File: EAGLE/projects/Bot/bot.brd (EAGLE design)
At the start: 122 x 94.9 mm, 19 parts, among them IC1 7805T, U3 ARDUINO_SHIELDLABEL

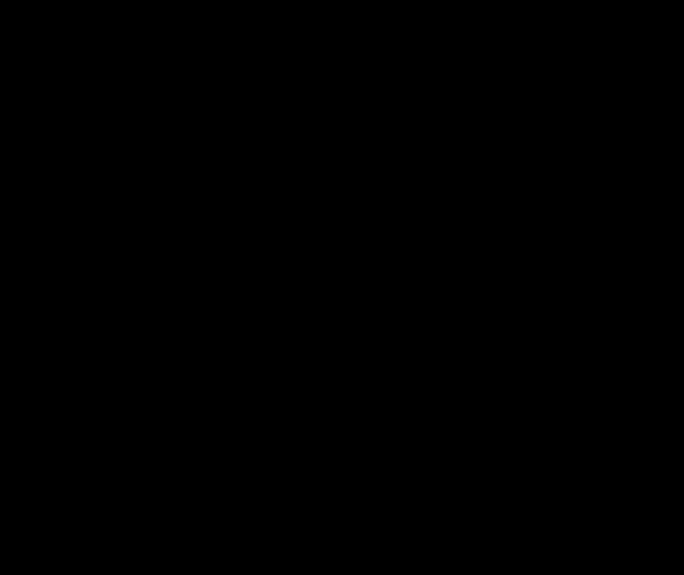
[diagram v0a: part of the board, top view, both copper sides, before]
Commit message: add blinker LED
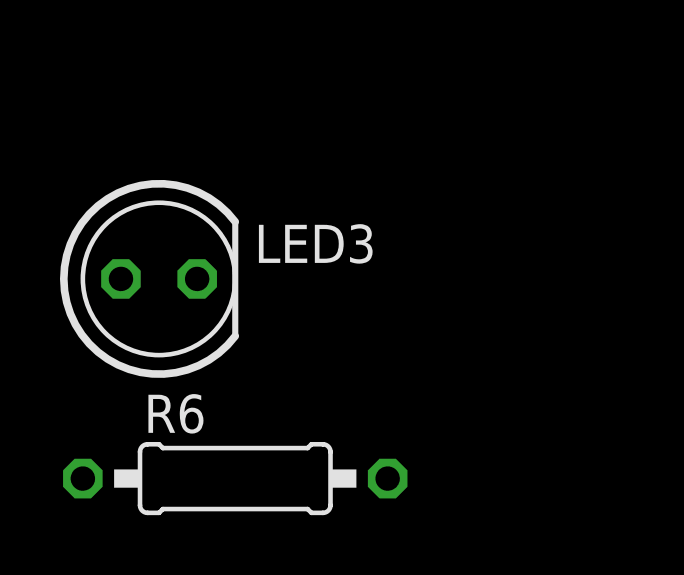
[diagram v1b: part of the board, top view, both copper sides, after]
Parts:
- added LED3: (no value), led:LED5MM
- added R6: 100, resistor:0207/10
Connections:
- new net N$4: LED3.A, PI.22
- new net N$6: LED3.K, R6.2
- net 0: now also R6.1
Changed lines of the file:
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@@
 <attribute name="VALUE" x="30.5562" y="21.1836" size="1.778" layer="27" ratio="10" rot="R180"/>
+</element>
+<element name="LED3" library="led" library_urn="urn:adsk.eagle:library:259" package="LED5MM" package3d_urn="urn:adsk.eagle:package:15799/2" value="" x="0.7112" y="-10.3124" smashed="yes">
+<attribute name="NAME" x="3.8862" y="-9.779" size="1.27" layer="25" ratio="10"/>
+<attribute name="POPULARITY" value="93" x="0.7112" y="-10.3124" size="1.778" layer="27" display="off"/>
+<attribute name="VALUE" x="3.9116" y="-12.1158" size="1.27" layer="27" ratio="10"/>
+</element>
+<element name="R6" library="resistor" library_urn="urn:adsk.eagle:library:348" package="0207/10" package3d_urn="urn:adsk.eagle:package:25939/1" value="100" x="3.2512" y="-16.9672" smashed="yes">
+<attribute name="NAME" x="0.2032" y="-15.4432" size="1.27" layer="25" ratio="10"/>
+<attribute name="VALUE" x="0.9906" y="-17.6022" size="1.27" layer="27" ratio="10"/>
 </element>
 </elements>
@@
 <wire x1="102.235" y1="25.4" x2="110.49" y2="25.4" width="0.3048" layer="16"/>
 <wire x1="26.035" y1="10.795" x2="25.5016" y2="11.0744" width="0.3048" layer="16"/>
+<contactref element="R6" pad="1"/>
+<wire x1="-1.8288" y1="-16.9672" x2="25.5016" y2="11.0744" width="0" layer="19" extent="1-1"/>
 </signal>
 <signal name="L_FWD">
@@
 </polygon>
 </signal>
+<signal name="N$4">
+<contactref element="PI" pad="22"/>
+<contactref element="LED3" pad="A"/>
+<wire x1="-0.5588" y1="-10.3124" x2="53.2366" y2="63.4118" width="0" layer="19" extent="1-1"/>
+</signal>
+<signal name="N$6">
+<contactref element="LED3" pad="K"/>
+<contactref element="R6" pad="2"/>
+<wire x1="8.3312" y1="-16.9672" x2="1.9812" y2="-10.3124" width="0" layer="19" extent="1-1"/>
+</signal>
 </signals>

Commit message: git
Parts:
- added S1: (no value), switch1:MS243
- moved R6 117.9 mm to (112.0, 28.5), turned to 90 degrees
- moved LED3 74.8 mm to (62.2, 32.2)
- moved JP7 4.80 mm to (107.5, 85.5)
- moved KK1 3.03 mm to (28.4, 14.4)
- moved IC1 3.03 mm to (28.4, 22.0)
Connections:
- new net N$3: JP2.1, S1.1
- net 0: now also S1.2; no longer JP2.1
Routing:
- net N$3: track 0.00 -> 77.8 mm
- net PI_5V: track 263.3 -> 317.0 mm
- net N$6: track 0.00 -> 52.3 mm, vias 0 -> 2
- net PI_3V3: track 79.8 -> 120.1 mm
- net N$4: track 0.00 -> 34.5 mm, vias 0 -> 2
- net 0: track 501.5 -> 477.6 mm
- net PWR+: track 241.3 -> 233.2 mm
- net L_SPD: track 53.2 -> 49.2 mm
- net R_SPD: track 93.6 -> 91.6 mm
- added copper zone on layer 16, net 0
- removed copper zone on layer 16, net N$3
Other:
- board size 122 x 94.9 mm -> 122.5 x 95 mm

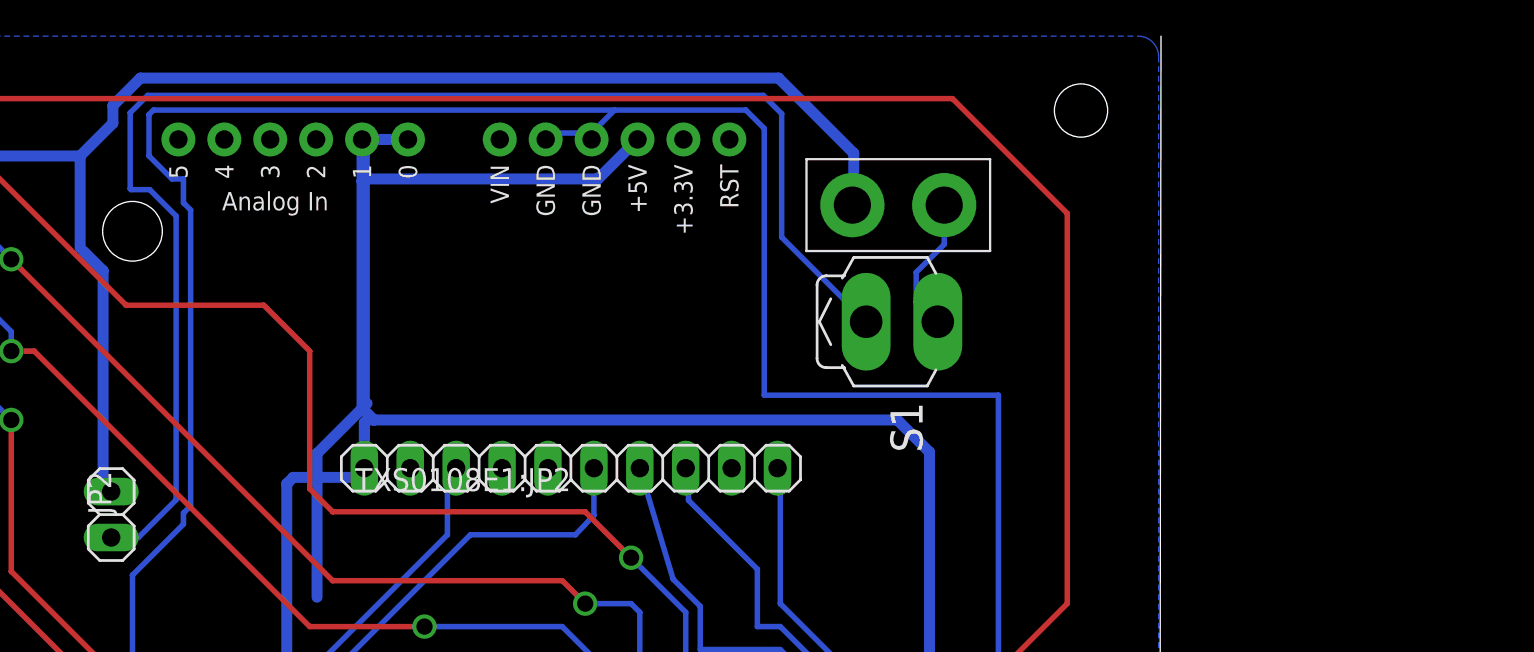
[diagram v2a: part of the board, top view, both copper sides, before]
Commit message: fixed switch position
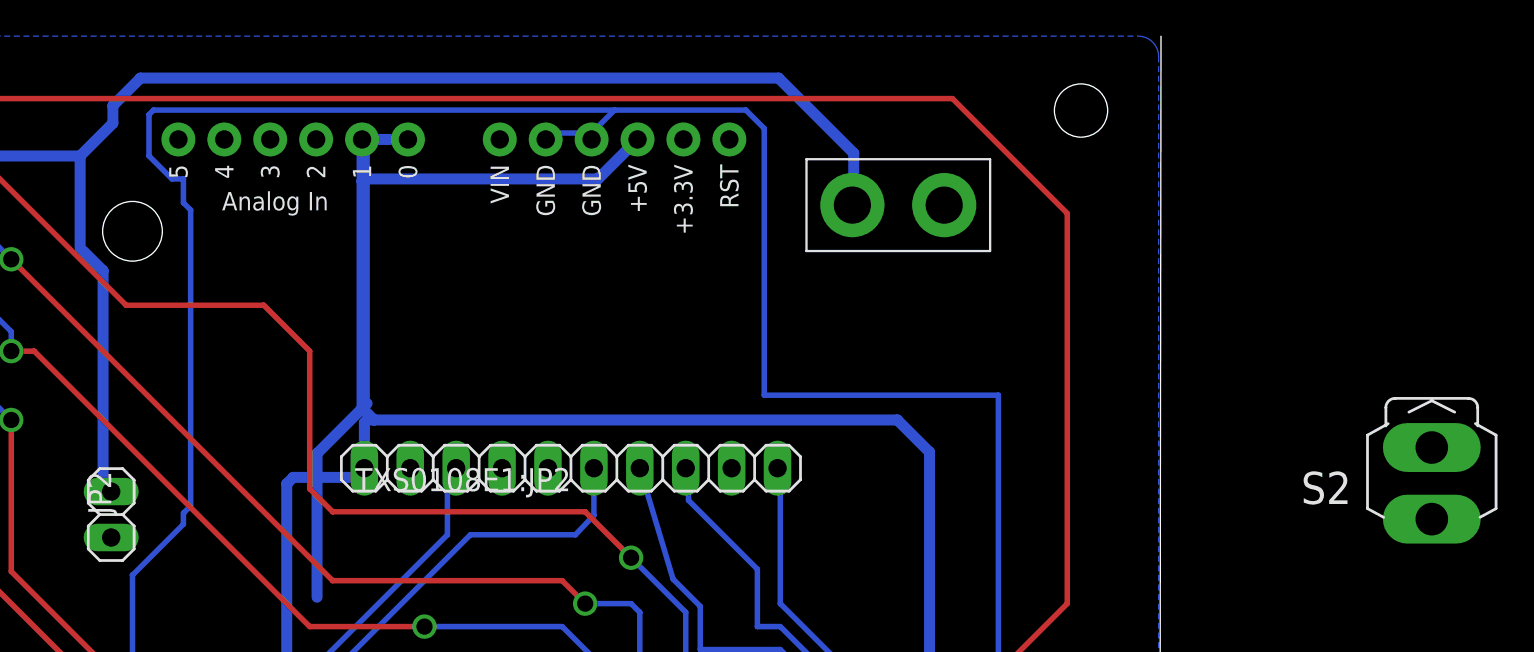
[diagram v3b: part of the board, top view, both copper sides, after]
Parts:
- removed S1: (no value), switch1:MS243
- added S2: (no value), switch1:MS243
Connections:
- removed net N$3: JP2.1, S1.1
- new net N$7: JP7.2, S2.1
- net 0: now also JP2.1, S2.2; no longer JP7.2, S1.2
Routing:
- net N$3: track 77.8 -> 0.00 mm
- net 0: track 477.6 -> 470.0 mm
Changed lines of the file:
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@@
 <attribute name="VALUE" x="112.6236" y="26.2128" size="1.27" layer="27" ratio="10" rot="R90"/>
 </element>
-<element name="S1" library="switch1" package="MS243" package3d_urn="urn:adsk.eagle:package:27683/1" value="" x="108.331" y="79.0956" smashed="yes" rot="R270">
-<attribute name="NAME" x="107.061" y="74.6506" size="1.778" layer="25" ratio="10" rot="R270"/>
-<attribute name="POPULARITY" value="3" x="108.331" y="79.0956" size="1.778" layer="27" rot="R270" display="off"/>
-<attribute name="VALUE" x="104.521" y="74.6506" size="1.778" layer="27" ratio="10" rot="R270"/>
+<element name="S2" library="switch1" package="MS243" package3d_urn="urn:adsk.eagle:package:27683/1" value="" x="137.0076" y="69.5198" smashed="yes" rot="R180">
+<attribute name="NAME" x="132.5626" y="70.7898" size="1.778" layer="25" ratio="10" rot="R180"/>
+<attribute name="POPULARITY" value="3" x="137.0076" y="69.5198" size="1.778" layer="27" rot="R180" display="off"/>
+<attribute name="VALUE" x="132.5626" y="73.3298" size="1.778" layer="27" ratio="10" rot="R180"/>
 </element>
 </elements>
@@
 <contactref element="U$2" pad="4"/>
 <contactref element="R5" pad="1"/>
-<contactref element="JP7" pad="2"/>
 <contactref element="U3" pad="GND@2"/>
 <contactref element="U3" pad="GND@1"/>
@@
 <wire x1="65.1256" y1="65.0748" x2="65.1256" y2="54.9656" width="0.3048" layer="16"/>
 <wire x1="53.34" y1="43.18" x2="65.1256" y2="54.9656" width="0.3048" layer="16"/>
-<contactref element="S1" pad="2"/>
-<wire x1="108.4834" y1="81.825725" x2="108.4834" y2="80.175475" width="0.3048" layer="16"/>
-<wire x1="108.4834" y1="80.175475" x2="108.572675" y2="80.0862" width="0.3048" layer="16"/>
-<wire x1="110.0328" y1="85.5472" x2="110.0328" y2="83.375125" width="0.3048" layer="16"/>
-<wire x1="110.0328" y1="83.375125" x2="108.4834" y2="81.825725" width="0.3048" layer="16"/>
-<wire x1="108.572675" y1="80.0862" x2="108.6866" y2="80.0862" width="0.3048" layer="16"/>
-<wire x1="108.6866" y1="80.0862" x2="109.6772" y2="79.0956" width="0.3048" layer="16"/>
 <wire x1="67.945" y1="67.8942" x2="65.1256" y2="65.0748" width="0.3048" layer="16"/>
 <wire x1="66.2891625" y1="90.805" x2="91.7956" y2="90.805" width="0.3048" layer="16"/>
@@
 <wire x1="90.5256" y1="89.1794" x2="90.5256" y2="89.535" width="0.3048" layer="16"/>
 <wire x1="90.5256" y1="89.535" x2="91.7956" y2="90.805" width="0.3048" layer="16"/>
-<wire x1="100.8126" y1="70.993" x2="109.6772" y2="79.0956" width="0" layer="19" extent="1-1"/>
+<contactref element="S2" pad="2"/>
+<contactref element="JP2" pad="1"/>
+<wire x1="100.8126" y1="70.993" x2="137.0076" y2="68.1736" width="0" layer="19" extent="1-1"/>
 <wire x1="111.9886" y1="23.3934" x2="96.1898" y2="23.3172" width="0" layer="19" extent="1-1"/>
+<wire x1="63.948453125" y1="67.1576" x2="65.1256" y2="65.1002" width="0" layer="19" extent="16-16"/>
 </signal>
 <signal name="L_FWD">
@@
 <wire x1="66.3956" y1="35.052" x2="63.5" y2="32.1564" width="0.3048" layer="16"/>
 </signal>
-<signal name="N$3">
-<contactref element="S1" pad="1"/>
-<contactref element="JP2" pad="1"/>
-<wire x1="105.7148" y1="79.0956" x2="101.0412" y2="83.7692" width="0.3048" layer="16"/>
-<wire x1="101.0412" y1="83.7692" x2="101.0412" y2="90.6018" width="0.3048" layer="16"/>
-<wire x1="101.0412" y1="90.6018" x2="100.0252" y2="91.6178" width="0.3048" layer="16"/>
-<wire x1="65.9638" y1="91.6178" x2="64.9986" y2="90.6526" width="0.3048" layer="16"/>
-<wire x1="64.9986" y1="90.6526" x2="64.9986" y2="86.4536" width="0.3048" layer="16"/>
-<wire x1="64.9986" y1="86.4536" x2="65.0494" y2="86.4028" width="0.3048" layer="16"/>
-<wire x1="65.0494" y1="86.4028" x2="66.0797" y2="86.4028" width="0.3048" layer="16"/>
-<wire x1="65.4558" y1="67.1576" x2="63.948453125" y2="67.1576" width="0.3048" layer="16"/>
-<wire x1="100.0252" y1="91.6178" x2="65.9638" y2="91.6178" width="0.3048" layer="16"/>
-<wire x1="66.0797" y1="86.4028" x2="67.5386" y2="84.9439" width="0.3048" layer="16"/>
-<wire x1="67.5386" y1="84.9439" x2="67.5386" y2="69.2404" width="0.3048" layer="16"/>
-<wire x1="67.5386" y1="69.2404" x2="65.4558" y2="67.1576" width="0.3048" layer="16"/>
+<signal name="N$7">
+<contactref element="JP7" pad="2"/>
+<contactref element="S2" pad="1"/>
+<wire x1="110.0328" y1="85.5472" x2="137.0076" y2="72.136" width="0" layer="19" extent="1-1"/>
 </signal>
 </signals>

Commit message: Shoot me!
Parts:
- S2: device switch1:MS243 -> switch2:MS243
- moved S2 32.2 mm to (106.2, 78.9), turned to 90 degrees
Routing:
- net PI_5V: track 317.0 -> 305.1 mm
- net N$7: track 0.00 -> 11.1 mm
- net 0: track 470.0 -> 473.7 mm
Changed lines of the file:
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@@
 <setting verticaltext="up"/>
 </settings>
-<grid distance="1" unitdist="mil" unit="mil" style="lines" multiple="1" display="no" altdistance="5" altunitdist="mil" altunit="mil"/>
+<grid distance="20" unitdist="mil" unit="mil" style="lines" multiple="1" display="no" altdistance="5" altunitdist="mil" altunit="mil"/>
 <layers>
 <layer number="1" name="Top" color="4" fill="1" visible="yes" active="yes"/>
@@
 <attribute name="VALUE" x="112.6236" y="26.2128" size="1.27" layer="27" ratio="10" rot="R90"/>
 </element>
-<element name="S2" library="switch1" package="MS243" package3d_urn="urn:adsk.eagle:package:27683/1" value="" x="137.0076" y="69.5198" smashed="yes" rot="R180">
-<attribute name="NAME" x="132.5626" y="70.7898" size="1.778" layer="25" ratio="10" rot="R180"/>
-<attribute name="POPULARITY" value="3" x="137.0076" y="69.5198" size="1.778" layer="27" rot="R180" display="off"/>
-<attribute name="VALUE" x="132.5626" y="73.3298" size="1.778" layer="27" ratio="10" rot="R180"/>
+<element name="S2" library="switch2" package="MS243" package3d_urn="urn:adsk.eagle:package:27683/1" value="" x="106.2228" y="78.9432" smashed="yes" rot="R90">
+<attribute name="NAME" x="107.4928" y="83.3882" size="1.778" layer="25" ratio="10" rot="R90"/>
+<attribute name="POPULARITY" value="3" x="106.2228" y="78.9432" size="1.778" layer="27" rot="R90" display="off"/>
+<attribute name="VALUE" x="110.0328" y="83.3882" size="1.778" layer="27" ratio="10" rot="R90"/>
 </element>
 </elements>
@@
 <wire x1="92.075" y1="22.86" x2="92.075" y2="12.7" width="0.3048" layer="16"/>
 <wire x1="53.2366" y1="43.0918" x2="53.34" y2="43.18" width="0.3048" layer="16"/>
-<wire x1="90.17" y1="89.535" x2="88.265" y2="89.535" width="0.3048" layer="16"/>
-<wire x1="88.265" y1="89.535" x2="87.9856" y2="89.1794" width="0.3048" layer="16"/>
-<wire x1="90.17" y1="89.535" x2="90.5256" y2="89.1794" width="0.3048" layer="16"/>
 <wire x1="102.235" y1="16.51" x2="107.315" y2="11.43" width="0.3048" layer="16"/>
 <wire x1="102.235" y1="31.115" x2="102.235" y2="25.4" width="0.3048" layer="16"/>
@@
 <wire x1="107.315" y1="11.43" x2="107.188" y2="10.8712" width="0.3048" layer="16"/>
 <wire x1="100.076" y1="75.0316" x2="113.03" y2="75.0316" width="0.3048" layer="16"/>
-<wire x1="90.805" y1="89.535" x2="90.5256" y2="89.1794" width="0.3048" layer="16"/>
 <wire x1="67.31" y1="86.995" x2="67.945" y2="86.995" width="0.3048" layer="16"/>
 <wire x1="66.04" y1="88.265" x2="67.31" y2="86.995" width="0.3048" layer="16"/>
@@
 <vertex x="-0.4826" y="93.740434375" curve="-90"/>
 </polygon>
-<wire x1="65.1256" y1="65.1002" x2="65.1256" y2="65.0748" width="0.3048" layer="16"/>
-<wire x1="65.1256" y1="65.0748" x2="65.1256" y2="54.9656" width="0.3048" layer="16"/>
+<wire x1="65.1256" y1="54.9656" x2="65.1256" y2="65.0748" width="0.3048" layer="16"/>
 <wire x1="53.34" y1="43.18" x2="65.1256" y2="54.9656" width="0.3048" layer="16"/>
 <wire x1="67.945" y1="67.8942" x2="65.1256" y2="65.0748" width="0.3048" layer="16"/>
-<wire x1="66.2891625" y1="90.805" x2="91.7956" y2="90.805" width="0.3048" layer="16"/>
-<wire x1="91.7956" y1="90.805" x2="99.06" y2="90.805" width="0.3048" layer="16"/>
+<wire x1="66.2891625" y1="90.805" x2="87.884" y2="90.805" width="0.3048" layer="16"/>
+<wire x1="87.884" y1="90.805" x2="99.06" y2="90.805" width="0.3048" layer="16"/>
 <wire x1="66.2891625" y1="90.805" x2="66.04" y2="90.5558375" width="0.3048" layer="16"/>
 <wire x1="66.04" y1="90.5558375" x2="66.04" y2="88.265" width="0.3048" layer="16"/>
@@
 <wire x1="100.076" y1="89.789" x2="100.076" y2="75.0316" width="0.3048" layer="16"/>
 <wire x1="99.06" y1="90.805" x2="100.076" y2="89.789" width="0.3048" layer="16"/>
-<wire x1="90.5256" y1="89.1794" x2="90.5256" y2="89.535" width="0.3048" layer="16"/>
-<wire x1="90.5256" y1="89.535" x2="91.7956" y2="90.805" width="0.3048" layer="16"/>
 <contactref element="S2" pad="2"/>
 <contactref element="JP2" pad="1"/>
-<wire x1="100.8126" y1="70.993" x2="137.0076" y2="68.1736" width="0" layer="19" extent="1-1"/>
-<wire x1="111.9886" y1="23.3934" x2="96.1898" y2="23.3172" width="0" layer="19" extent="1-1"/>
-<wire x1="63.948453125" y1="67.1576" x2="65.1256" y2="65.1002" width="0" layer="19" extent="16-16"/>
+<wire x1="65.1256" y1="65.0748" x2="65.1256" y2="65.980453125" width="0.3048" layer="16"/>
+<wire x1="65.1256" y1="65.980453125" x2="63.948453125" y2="67.1576" width="0.3048" layer="16"/>
+<wire x1="104.1908" y1="78.9432" x2="105.4608" y2="78.9432" width="0.3048" layer="16"/>
+<wire x1="105.4608" y1="78.9432" x2="106.172" y2="78.232" width="0.3048" layer="16"/>
+<wire x1="105.156" y1="71.12" x2="105.029" y2="70.993" width="0.3048" layer="16"/>
+<wire x1="87.9856" y1="89.1794" x2="87.884" y2="89.281" width="0.3048" layer="16"/>
+<wire x1="87.884" y1="89.281" x2="87.884" y2="90.805" width="0.3048" layer="16"/>
+<wire x1="90.5256" y1="89.1794" x2="87.9856" y2="89.1794" width="0.3048" layer="16"/>
 </signal>
 <signal name="L_FWD">
@@
 <wire x1="77.9526" y1="70.993" x2="77.47" y2="70.5104" width="0.6096" layer="16"/>
 <wire x1="77.47" y1="70.5104" x2="77.47" y2="70.485" width="0.6096" layer="16"/>
-<wire x1="78.105" y1="74.5744" x2="75.3364" y2="71.8058" width="0.6096" layer="16"/>
-<wire x1="75.3364" y1="71.8058" x2="75.3364" y2="63.8556" width="0.6096" layer="16"/>
 </signal>
 <signal name="N$1">
@@
 <contactref element="JP7" pad="2"/>
 <contactref element="S2" pad="1"/>
-<wire x1="110.0328" y1="85.5472" x2="137.0076" y2="72.136" width="0" layer="19" extent="1-1"/>
+<wire x1="108.2548" y1="78.9432" x2="107.442" y2="79.756" width="0.3048" layer="16"/>
+<wire x1="107.442" y1="79.756" x2="106.426" y2="79.756" width="0.3048" layer="16"/>
+<wire x1="106.426" y1="79.756" x2="106.1974" y2="79.9846" width="0.3048" layer="16"/>
+<wire x1="106.1974" y1="79.9846" x2="106.1974" y2="82.0674" width="0.3048" layer="16"/>
+<wire x1="106.1974" y1="82.0674" x2="106.5022" y2="82.3722" width="0.3048" layer="16"/>
+<wire x1="106.5022" y1="82.3722" x2="108.9152" y2="82.3722" width="0.3048" layer="16"/>
+<wire x1="108.9152" y1="82.3722" x2="110.0328" y2="83.4898" width="0.3048" layer="16"/>
+<wire x1="110.0328" y1="83.4898" x2="110.0328" y2="85.5472" width="0.3048" layer="16"/>
 </signal>
 </signals>
